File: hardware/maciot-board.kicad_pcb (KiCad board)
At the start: 2 copper layers, 68.6 x 53.3 mm, 74 parts, among them P1 Power, P101 USB_OTG, P102 TST, P103 TST, P104 TST, P105 TST, P106 TST, P107 TST, P108 TST, P109 TST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

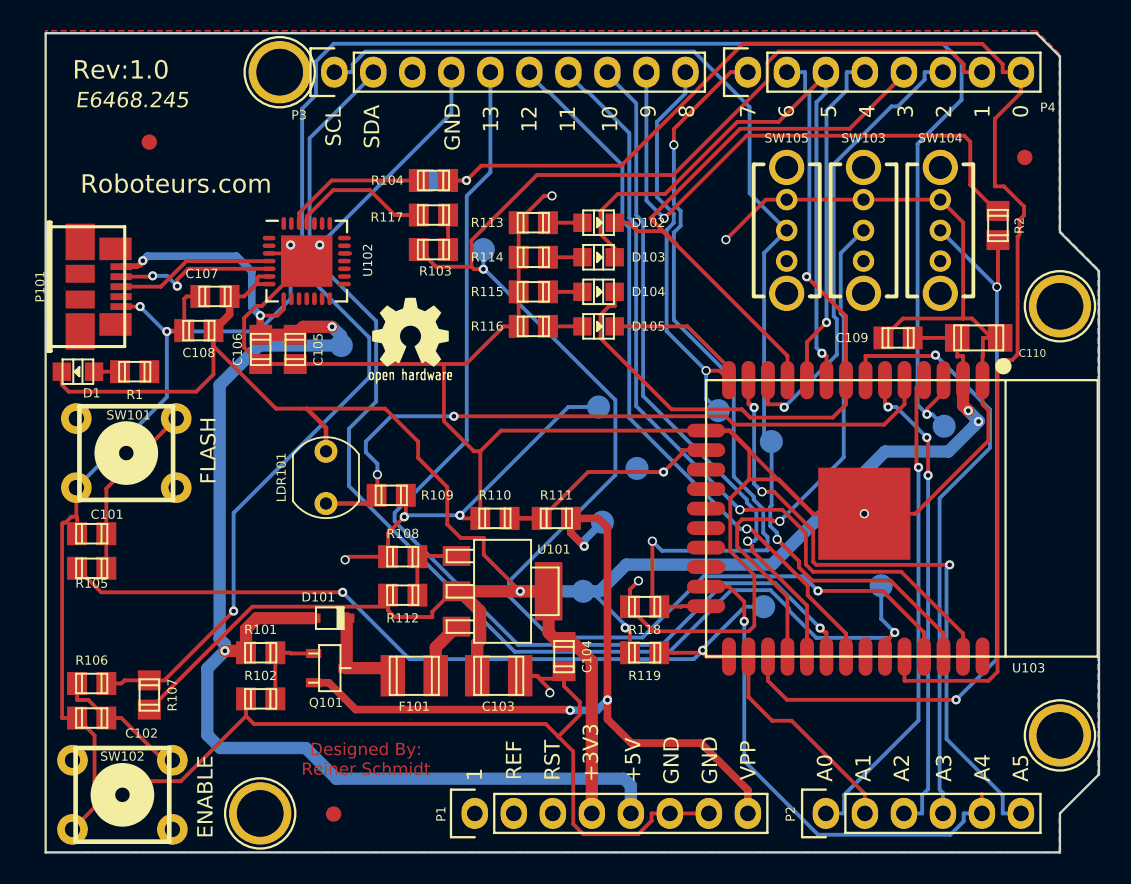
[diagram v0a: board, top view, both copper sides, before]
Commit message: added cap pad
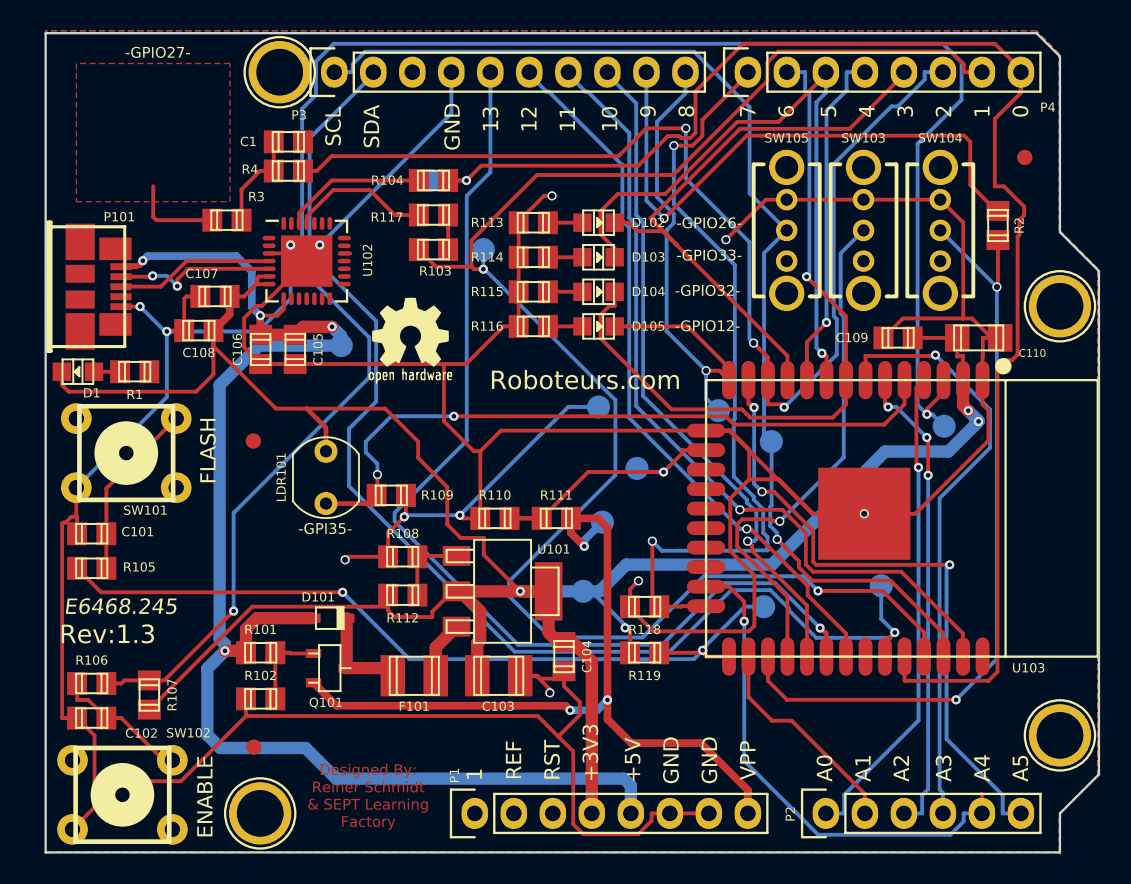
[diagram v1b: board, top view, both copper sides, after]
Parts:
- added C1: 10nf, w_smd_cap:c_0805, F.Cu at (126.8, 80.1)
- added R3: 0, w_smd_resistors:r_0805, F.Cu at (122.8, 85.2)
- added R4: 0, w_smd_resistors:r_0805, F.Cu at (126.8, 82.0)
- moved FD1 20.6 mm to (124.5, 99.6)
- moved FD3 6.77 mm to (124.6, 119.5)
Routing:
- net /2: track 29.9 -> 74.6 mm, vias 1 -> 3
- net Net-(C1-Pad2): track 0.00 -> 6.50 mm
- net Net-(R3-Pad2): track 0.00 -> 5.93 mm
- net /0(Rx): track 94.1 -> 95.6 mm
- added copper zone on F.Cu, net Net-(R3-Pad2)
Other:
- board text added: "-GPI35-"
- board text added: "-GPIO12-"
- board text added: "-GPIO26-"
- board text added: "-GPIO27-"
- board text added: "-GPIO32-"
- board text added: "-GPIO33-"
- board text added: "Designed By: Reiner Schmidt & SEPT Learning Factory"
- board text added: "Rev:1.3"
- board text removed: "Designed By: Reiner Schmidt"
- board text removed: "Rev:1.0"
